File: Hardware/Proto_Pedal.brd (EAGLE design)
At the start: 85.1 x 110.5 mm, 124 parts, among them Q1 2.5A/30V

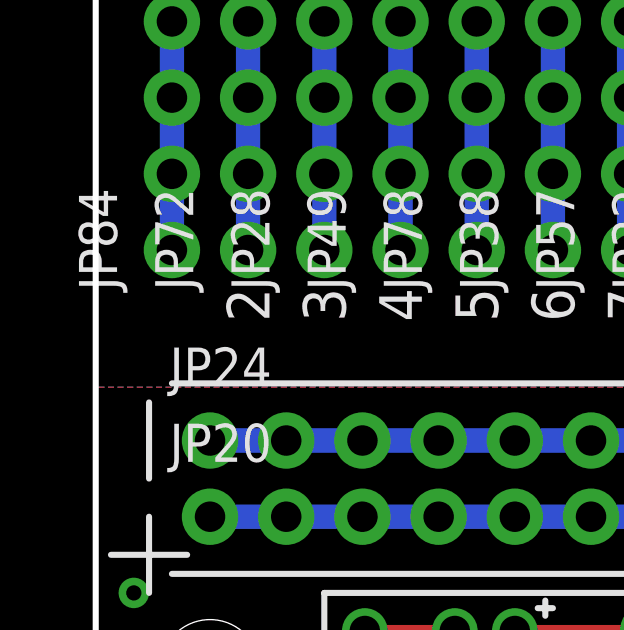
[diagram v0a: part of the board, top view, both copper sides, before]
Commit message: A couple of fixes after review.
Fixed spelling of sililar.
One piece of top silk had fallen to bottom - now corrected.
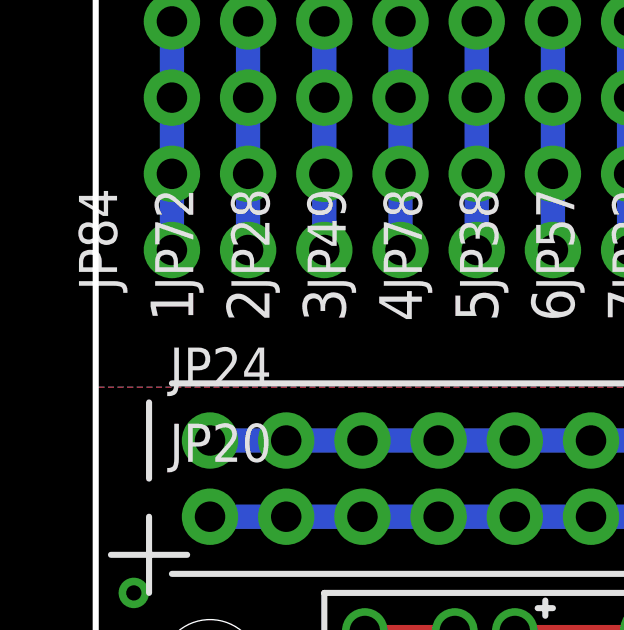
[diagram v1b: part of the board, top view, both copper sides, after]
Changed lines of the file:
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@@
 <text x="73.66" y="67.31" size="1.4224" layer="21" font="vector" ratio="15" rot="R90" align="center-left">29</text>
 <text x="76.2" y="67.31" size="1.4224" layer="21" font="vector" ratio="15" rot="R90" align="center-left">30</text>
-<text x="2.54" y="36.83" size="1.4224" layer="22" font="vector" ratio="15" rot="MR90" align="center-right">1</text>
+<text x="2.54" y="36.83" size="1.4224" layer="21" font="vector" ratio="15" rot="R90" align="center-right">1</text>
 <text x="5.08" y="36.83" size="1.4224" layer="21" font="vector" ratio="15" rot="R90" align="center-right">2</text>
 <text x="7.62" y="36.83" size="1.4224" layer="21" font="vector" ratio="15" rot="R90" align="center-right">3</text>

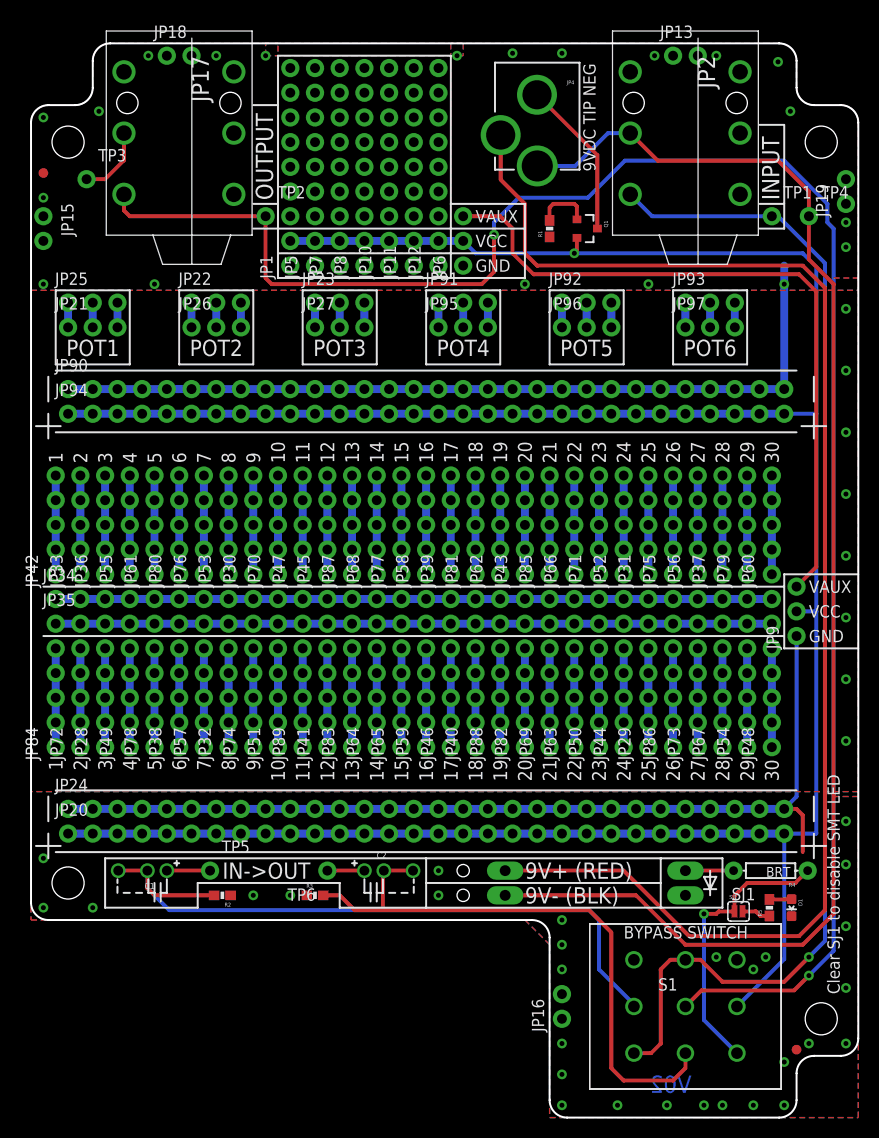
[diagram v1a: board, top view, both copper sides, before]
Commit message: Updates based on proto evaluation.
Usability & fit'n'finish issues solved.
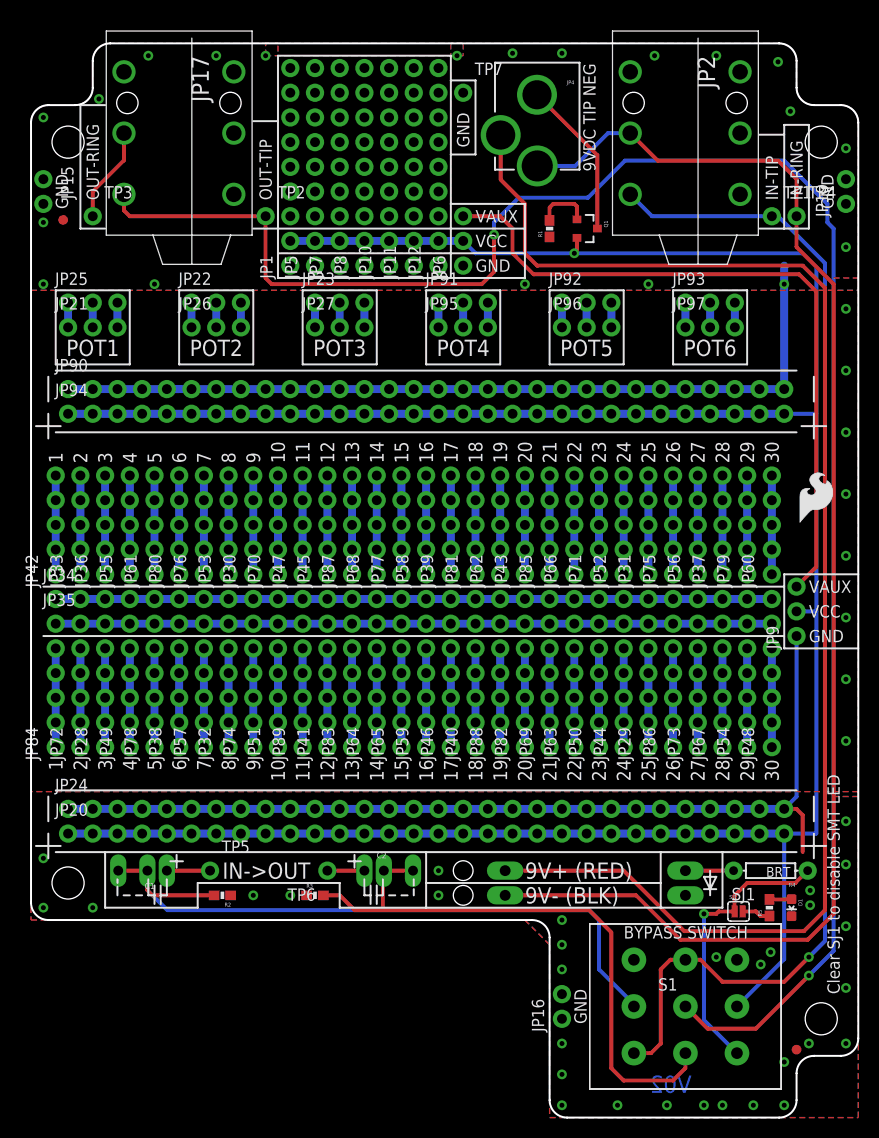
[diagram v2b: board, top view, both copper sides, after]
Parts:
- removed JP13, JP18: 1x2, SparkFun-Connectors:1X02_NO_SILK
- added LOGO3: SFE_LOGO_FLAME.2_INCH, SparkFun-Aesthetics:SFE_LOGO_FLAME_.2
- added TP7: Out Ring, SparkFun-Connectors:1X01_NO_SILK
- moved FID2 5.24 mm to (3.30, 92.3)
- moved TP3 3.86 mm to (6.35, 92.7)
- moved JP15 3.81 mm to (1.27, 96.5)
- moved TP4 1.27 mm to (78.7, 92.7)
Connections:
- net GND: now also TP7.1; no longer JP13.1, JP13.2, JP18.1, JP18.2, JP2.TIP-NORM
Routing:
- net N$66: track 7.45 -> 9.88 mm
- net N$71: track 185.6 -> 187.5 mm
- net GND: vias 57 -> 59
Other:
- board text added: "IN-RING"
- board text added: "IN-TIP"
- board text added: "OUT-RING"
- board text added: "OUT-TIP"
- board text added: "Stomp switch needs 0.5" hole in chassis"
- board text removed: "INPUT"
- board text removed: "OUTPUT"
- board text removed: "Stomp switch needs 0.5" hole"

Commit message: PCB updates after Marshall looked closer.
A new more nits cleaned up.
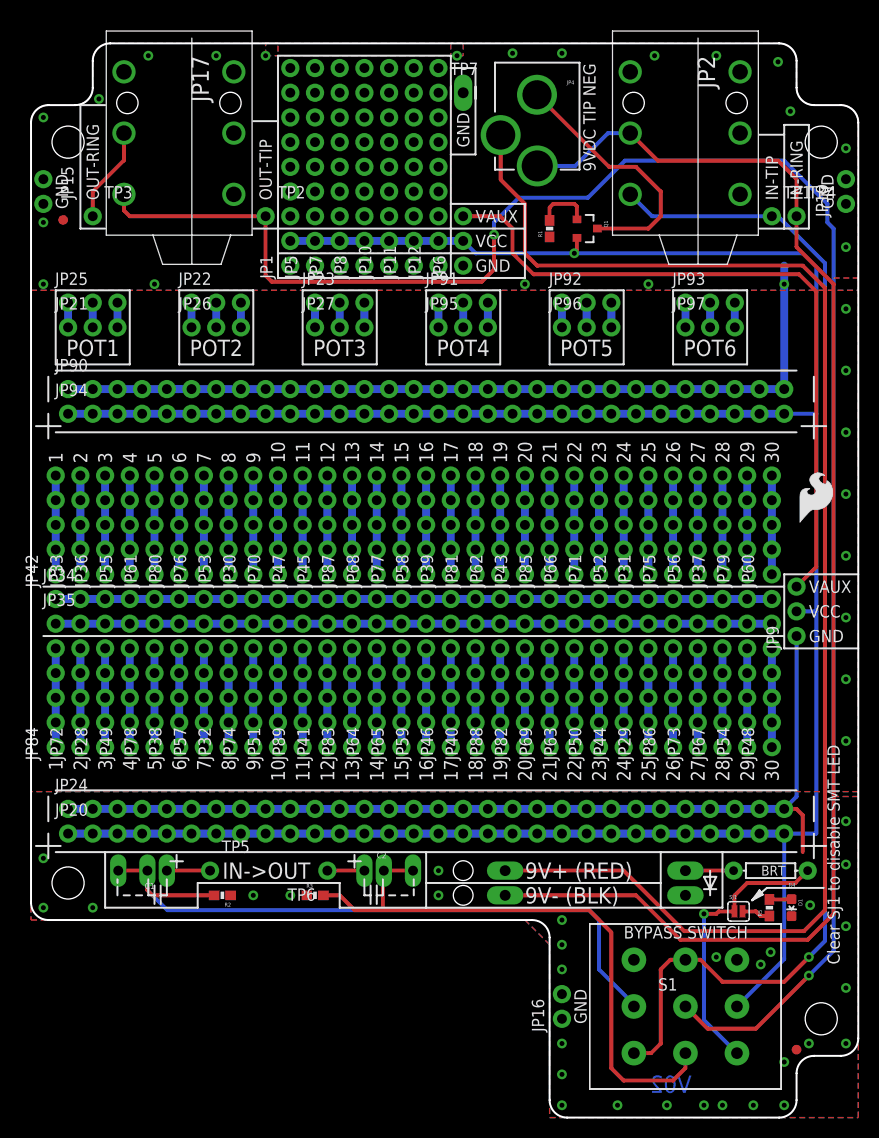
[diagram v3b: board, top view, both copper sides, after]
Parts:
- TP7: device SparkFun-Connectors:1X01_NO_SILK -> SparkFun-Connectors:1X01_LONGPAD
- moved LOGO1 2.54 mm to (80.6, 85.7)
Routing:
- net VBATT: track 16.3 -> 26.4 mm
- net N$71: track 187.5 -> 187.0 mm
- net GND: vias 59 -> 58
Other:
- board text removed: "SJ1"
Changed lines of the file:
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@@
 <setting verticaltext="up"/>
 </settings>
-<grid distance="0.01" unitdist="inch" unit="inch" style="lines" multiple="1" display="yes" altdistance="0.001" altunitdist="inch" altunit="inch"/>
+<grid distance="0.05" unitdist="inch" unit="inch" style="lines" multiple="1" display="yes" altdistance="0.005" altunitdist="inch" altunit="inch"/>
 <layers>
 <layer number="1" name="Top" color="4" fill="1" visible="yes" active="yes"/>
@@
 <wire x1="47.625" y1="108.839" x2="46.355" y2="108.839" width="0.254" layer="22"/>
 <text x="22.86" y="87.63" size="2.1844" layer="22" font="vector" ratio="15" rot="MR0">Proto Pedal</text>
-<text x="73.279" y="22.352" size="1.27" layer="21" font="vector" ratio="15" align="bottom-center">SJ1</text>
-<text x="82.55" y="12.7" size="1.27" layer="21" font="vector" ratio="15" rot="R90" align="center-left">Clear SJ1 to disable SMT LED</text>
+<text x="82.55" y="15.748" size="1.27" layer="21" font="vector" ratio="15" rot="R90" align="center-left">Clear SJ1 to disable SMT LED</text>
 <wire x1="43.18" y1="86.36" x2="50.8" y2="86.36" width="0.2032" layer="21"/>
 <wire x1="43.18" y1="93.98" x2="50.8" y2="93.98" width="0.2032" layer="21"/>
@@
 <wire x1="25.4" y1="102.489" x2="25.4" y2="109.22" width="0.2032" layer="21"/>
 <wire x1="25.4" y1="109.22" x2="43.18" y2="109.22" width="0.2032" layer="21"/>
-<wire x1="43.18" y1="109.22" x2="43.18" y2="106.68" width="0.2032" layer="21"/>
+<wire x1="43.18" y1="109.22" x2="43.18" y2="107.95" width="0.2032" layer="21"/>
 <hole x="44.45" y="22.86" drill="2.032"/>
 <hole x="44.45" y="25.4" drill="2.032"/>
-<wire x1="43.18" y1="106.68" x2="43.18" y2="99.06" width="0.2032" layer="21"/>
+<wire x1="43.18" y1="107.95" x2="43.18" y2="99.06" width="0.2032" layer="21"/>
 <wire x1="43.18" y1="99.06" x2="43.18" y2="93.98" width="0.2032" layer="21"/>
 <wire x1="43.18" y1="109.22" x2="25.4" y2="109.22" width="0.2032" layer="22"/>
 <wire x1="25.4" y1="109.22" x2="25.4" y2="102.489" width="0.2032" layer="22"/>
 <wire x1="43.18" y1="93.98" x2="43.18" y2="99.06" width="0.2032" layer="22"/>
-<wire x1="43.18" y1="99.06" x2="43.18" y2="106.68" width="0.2032" layer="22"/>
-<wire x1="43.18" y1="106.68" x2="43.18" y2="109.22" width="0.2032" layer="22"/>
+<wire x1="43.18" y1="99.06" x2="43.18" y2="107.95" width="0.2032" layer="22"/>
+<wire x1="43.18" y1="107.95" x2="43.18" y2="109.22" width="0.2032" layer="22"/>
 <wire x1="43.18" y1="91.44" x2="25.4" y2="91.44" width="0.2032" layer="22"/>
 <wire x1="43.18" y1="86.36" x2="25.4" y2="86.36" width="0.2032" layer="22"/>
@@
 <text x="44.45" y="103.378" size="1.27" layer="21" font="vector" ratio="15" rot="R270" align="center-left">GND</text>
 <text x="44.45" y="103.378" size="1.27" layer="22" font="vector" ratio="15" rot="MR90" align="center-right">GND</text>
-<wire x1="43.18" y1="106.68" x2="45.72" y2="106.68" width="0.2032" layer="21"/>
+<wire x1="43.18" y1="107.95" x2="45.72" y2="107.95" width="0.2032" layer="21"/>
 <wire x1="43.18" y1="99.06" x2="45.72" y2="99.06" width="0.2032" layer="21"/>
-<wire x1="45.72" y1="99.06" x2="45.72" y2="106.68" width="0.2032" layer="21"/>
-<wire x1="45.72" y1="106.68" x2="43.18" y2="106.68" width="0.2032" layer="22"/>
-<wire x1="45.72" y1="99.06" x2="45.72" y2="106.68" width="0.2032" layer="22"/>
+<wire x1="45.72" y1="99.06" x2="45.72" y2="107.95" width="0.2032" layer="21"/>
+<wire x1="45.72" y1="107.95" x2="43.18" y2="107.95" width="0.2032" layer="22"/>
+<wire x1="45.72" y1="99.06" x2="45.72" y2="107.95" width="0.2032" layer="22"/>
 <wire x1="45.72" y1="99.06" x2="43.18" y2="99.06" width="0.2032" layer="22"/>
 <wire x1="80.01" y1="91.44" x2="80.01" y2="102.108" width="0.2032" layer="22"/>
@@
 <wire x1="7.62" y1="104.14" x2="5.08" y2="104.14" width="0.2032" layer="21"/>
 <wire x1="5.08" y1="104.14" x2="7.62" y2="104.14" width="0.2032" layer="22"/>
+<wire x1="74.168" y1="22.352" x2="75.692" y2="23.622" width="0.2032" layer="21"/>
+<wire x1="75.692" y1="23.622" x2="81.534" y2="23.622" width="0.2032" layer="21"/>
+<wire x1="74.168" y1="22.352" x2="74.93" y2="23.368" width="0.2032" layer="21"/>
+<wire x1="74.93" y1="23.368" x2="75.2602" y2="22.9362" width="0.2032" layer="21"/>
+<wire x1="74.168" y1="22.352" x2="75.2602" y2="22.9362" width="0.2032" layer="21"/>
+<wire x1="74.7268" y1="22.987" x2="74.93" y2="23.1648" width="0.254" layer="21"/>
+<wire x1="74.93" y1="23.1648" x2="75.0316" y2="22.987" width="0.254" layer="21"/>
 </plain>
 <attributes>
@@
 <element name="JP97" library="SparkFun-Connectors" package="1X03_NO_SILK" value="1x3" x="67.31" y="81.28"/>
 <element name="JP9" library="SparkFun-Connectors" package="1X03_NO_SILK" value="1x3" x="78.74" y="49.53" rot="R90"/>
-<element name="LOGO1" library="SparkFun-Aesthetics" package="SFE_LOGO_NAME_FLAME_.2" value="SFE_LOGO_NAME_FLAME.2_INCH" x="83.185" y="85.725" rot="MR0"/>
+<element name="LOGO1" library="SparkFun-Aesthetics" package="SFE_LOGO_NAME_FLAME_.2" value="SFE_LOGO_NAME_FLAME.2_INCH" x="80.645" y="85.725" rot="MR0"/>
 <element name="LOGO2" library="SparkFun-Aesthetics" package="OSHW-LOGO-L" value="OSHW-LOGOL" x="15.24" y="99.06" rot="MR0"/>
 <element name="STANDOFF1" library="SparkFun-Electromechanical" package="STAND-OFF" value="STAND-OFF" x="81.28" y="10.16"/>
@@
 <element name="JP11" library="SparkFun-Connectors" package="1X09_NO_SILK" value="1x9" x="39.37" y="87.63" rot="R90"/>
 <element name="JP12" library="SparkFun-Connectors" package="1X09_NO_SILK" value="1x9" x="41.91" y="87.63" rot="R90"/>
-<element name="R4" library="SparkFun-Resistors" package="AXIAL-0.3" value="BRT" x="76.073" y="25.4" rot="R180"/>
+<element name="R4" library="SparkFun-Resistors" package="AXIAL-0.3" value="BRT" x="76.073" y="25.4" smashed="yes" rot="R180">
+<attribute name="NAME" x="78.613" y="24.13" size="0.4064" layer="25" font="vector" rot="R180"/>
+<attribute name="VALUE" x="77.597" y="25.908" size="1.016" layer="21" font="vector" ratio="15" rot="R180"/>
+</element>
 <element name="TP3" library="SparkFun-Connectors" package="1X01_NO_SILK" value="Out Ring" x="6.35" y="92.71"/>
 <element name="TP4" library="SparkFun-Connectors" package="1X01_NO_SILK" value="In Ring" x="78.74" y="92.71"/>
@@
 <attribute name="PROD_ID" value="CONN-08197" x="52.07" y="111.76" size="1.778" layer="27" rot="R180" display="off"/>
 </element>
-<element name="TP7" library="SparkFun-Connectors" package="1X01_NO_SILK" value="Out Ring" x="44.45" y="105.41"/>
+<element name="TP7" library="SparkFun-Connectors" package="1X01_LONGPAD" value="Out Ring" x="44.45" y="105.41"/>
 <element name="LOGO3" library="SparkFun-Aesthetics" package="SFE_LOGO_FLAME_.2" value="SFE_LOGO_FLAME.2_INCH" x="78.74" y="60.96"/>
 </elements>
@@
 <vertex x="24.13" y="110.49"/>
 </polygon>
-<via x="80.137" y="23.368" extent="1-16" drill="0.508"/>
 <via x="76.073" y="17.018" extent="1-16" drill="0.508"/>
 <via x="70.485" y="16.51" extent="1-16" drill="0.508"/>
@@
 <wire x1="9.56" y1="93.31" x2="10.16" y2="92.71" width="0.4064" layer="1"/>
 <wire x1="10.16" y1="92.71" x2="24.13" y2="92.71" width="0.4064" layer="1"/>
-<wire x1="24.13" y1="92.71" x2="24.13" y2="86.36" width="0.4064" layer="1"/>
-<wire x1="24.13" y1="86.36" x2="24.765" y2="85.725" width="0.4064" layer="1"/>
-<wire x1="24.765" y1="85.725" x2="46.355" y2="85.725" width="0.4064" layer="1"/>
-<wire x1="46.355" y1="85.725" x2="47.625" y2="86.995" width="0.4064" layer="1"/>
-<wire x1="47.625" y1="86.995" x2="47.625" y2="90.805" width="0.4064" layer="1"/>
+<wire x1="24.13" y1="92.71" x2="24.13" y2="86.614" width="0.4064" layer="1"/>
+<wire x1="24.13" y1="86.614" x2="24.765" y2="85.979" width="0.4064" layer="1"/>
+<wire x1="24.765" y1="85.979" x2="46.355" y2="85.979" width="0.4064" layer="1"/>
+<wire x1="46.355" y1="85.979" x2="47.625" y2="87.249" width="0.4064" layer="1"/>
+<wire x1="47.625" y1="87.249" x2="47.625" y2="90.805" width="0.4064" layer="1"/>
 <via x="47.625" y="90.805" extent="1-16" drill="0.508"/>
 <wire x1="47.625" y1="90.805" x2="47.625" y2="92.075" width="0.4064" layer="16"/>
@@
 <contactref element="Q1" pad="3"/>
 <contactref element="JP4" pad="SLEEVE"/>
-<wire x1="52.0446" y1="105.203" x2="58.25" y2="98.9976" width="0.4064" layer="1"/>
-<wire x1="58.25" y1="98.9976" x2="58.25" y2="91.44" width="0.4064" layer="1"/>
+<wire x1="52.0446" y1="105.203" x2="59.4576" y2="97.79" width="0.4064" layer="1"/>
+<wire x1="58.25" y1="91.44" x2="63.5" y2="91.44" width="0.4064" layer="1"/>
+<wire x1="63.5" y1="91.44" x2="64.77" y2="92.71" width="0.4064" layer="1"/>
+<wire x1="64.77" y1="92.71" x2="64.77" y2="95.25" width="0.4064" layer="1"/>
+<wire x1="64.77" y1="95.25" x2="62.23" y2="97.79" width="0.4064" layer="1"/>
+<wire x1="62.23" y1="97.79" x2="59.4576" y2="97.79" width="0.4064" layer="1"/>
 </signal>
 <signal name="N$75">
